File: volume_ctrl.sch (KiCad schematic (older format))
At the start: 40 parts, among them U1 TL072, U2 NE5532, U3 NE5532, U4 THAT2180

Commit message: Layout progress
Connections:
- net vca_in_R: now reaches R26.2, U4.1 (-)
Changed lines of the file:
@@
 EESchema Schematic File Version 4
+LIBS:AAMB-cache
 EELAYER 30 0
 EELAYER END
@@
 	1    0    0    -1
 $EndComp
+Text Label 6200 2425 0    50   ~ 0
+vca_in_R
 $EndSCHEMATC

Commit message: Lots of part changes to SMD devices. Adding MPN, MFG to all parts for BOM export.
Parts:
- C10, C9: MFG (none) -> Panasonic Electronic Components; MPN (none) -> EEV-FK1E102Q
- C11, C12: DigiKey (none) -> https://www.digikey.com/product-detail/en/w%C3%BCrth-elektr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; MFG (none) -> Würth Elektronik; MPN (none) -> 885012006053
- C13, C14, C7, C8: footprint Capacitor_THT:CP_Radial_D5.0mm_P2.00mm -> Capacitor_SMD:CP_Elec_5x3; DigiKey (none) -> https://www.digikey.com/product-detail/en/w%C3%BCrth-elektr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; MFG (none) -> Würth Elektronik; MPN (none) -> 865080642006
- C15, C16, C17, C18, C19, C20, C21, C22: MFG (none) -> KEMET; MPN (none) -> C0603C104Z3VACTU
- U4: MFG (none) -> Mill-Max Manufacturing Corp.; MPN (none) -> 214-99-316-01-670800
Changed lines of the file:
@@
 F 1 "THAT2180" H 6900 5100 50  0000 L CNN
 F 2 "Package_DIP:DIP-16_W7.62mm_SMDSocket_SmallPads" H 7100 4475 50  0001 C CNN
-F 3 "" H 7250 5275 50  0001 C CNN
+F 3 "https://www.mill-max.com/assets/pdfs/metric/108M.pdf" H 7250 5275 50  0001 C CNN
 F 4 "https://www.digikey.com/product-detail/en/mill-max-manufacturing-corp/214-99-316-01-670800/ED2130-ND/9895" H 6700 5225 50  0001 C CNN "DigiKey"
+F 5 "Mill-Max Manufacturing Corp." H 6700 5225 50  0001 C CNN "MFG"
+F 6 "214-99-316-01-670800" H 6700 5225 50  0001 C CNN "MPN"
 	2    6700 5225
 	1    0    0    -1
@@
 F 1 "THAT2180" H 6900 2300 50  0000 L CNN
 F 2 "Package_DIP:DIP-16_W7.62mm_SMDSocket_SmallPads" H 7100 1675 50  0001 C CNN
-F 3 "" H 7250 2475 50  0001 C CNN
+F 3 "https://www.mill-max.com/assets/pdfs/metric/108M.pdf" H 7250 2475 50  0001 C CNN
 F 4 "https://www.digikey.com/product-detail/en/mill-max-manufacturing-corp/214-99-316-01-670800/ED2130-ND/9895" H 6700 2425 50  0001 C CNN "DigiKey"
+F 5 "Mill-Max Manufacturing Corp." H 6700 2425 50  0001 C CNN "MFG"
+F 6 "214-99-316-01-670800" H 6700 2425 50  0001 C CNN "MPN"
 	1    6700 2425
 	1    0    0    -1
@@
 F 0 "C8" V 5370 5225 50  0000 C CNN
 F 1 "10u" V 5461 5225 50  0000 C CNN
-F 2 "Capacitor_THT:CP_Radial_D5.0mm_P2.00mm" H 5663 5075 50  0001 C CNN
-F 3 "~" H 5625 5225 50  0001 C CNN
+F 2 "Capacitor_SMD:CP_Elec_5x3" H 5663 5075 50  0001 C CNN
+F 3 "https://www.we-online.de/katalog/datasheet/865080642006.pdf" H 5625 5225 50  0001 C CNN
+F 4 "https://www.digikey.com/product-detail/en/w%C3%BCrth-elektronik/865080642006/732-8451-1-ND/5728408" H 5625 5225 50  0001 C CNN "DigiKey"
+F 5 "Würth Elektronik" H 5625 5225 50  0001 C CNN "MFG"
+F 6 "865080642006" H 5625 5225 50  0001 C CNN "MPN"
 	1    5625 5225
 	0    1    1    0
@@
 F 1 "22p" V 7500 5550 50  0000 C CNN
 F 2 "Capacitor_SMD:C_0603_1608Metric_Pad1.05x0.95mm_HandSolder" H 7763 5400 50  0001 C CNN
-F 3 "~" H 7725 5550 50  0001 C CNN
+F 3 "https://katalog.we-online.de/pbs/datasheet/885012006053.pdf" H 7725 5550 50  0001 C CNN
+F 4 "https://www.digikey.com/product-detail/en/w%C3%BCrth-elektronik/885012006053/732-7795-1-ND/5454422" H 7725 5550 50  0001 C CNN "DigiKey"
+F 5 "Würth Elektronik" H 7725 5550 50  0001 C CNN "MFG"
+F 6 "885012006053" H 7725 5550 50  0001 C CNN "MPN"
 	1    7725 5550
 	0    1    -1   0
@@
 F 0 "C14" V 9005 4850 50  0000 C CNN
 F 1 "10u" V 8914 4850 50  0000 C CNN
-F 2 "Capacitor_THT:CP_Radial_D5.0mm_P2.00mm" H 8788 4700 50  0001 C CNN
-F 3 "~" H 8750 4850 50  0001 C CNN
+F 2 "Capacitor_SMD:CP_Elec_5x3" H 8788 4700 50  0001 C CNN
+F 3 "https://www.we-online.de/katalog/datasheet/865080642006.pdf" H 8750 4850 50  0001 C CNN
+F 4 "https://www.digikey.com/product-detail/en/w%C3%BCrth-elektronik/865080642006/732-8451-1-ND/5728408" H 8750 4850 50  0001 C CNN "DigiKey"
+F 5 "Würth Elektronik" H 8750 4850 50  0001 C CNN "MFG"
+F 6 "865080642006" H 8750 4850 50  0001 C CNN "MPN"
 	1    8750 4850
 	0    -1   -1   0
@@
 F 3 "https://na.industrial.panasonic.com/file-download/3122" H 5850 3300 50  0001 C CNN
 F 4 "https://www.digikey.com/product-detail/en/panasonic-electronic-components/EEV-FK1E102Q/PCE3462TR-ND/396274" H 5850 3300 50  0001 C CNN "DigiKey"
+F 5 "Panasonic Electronic Components" H 5850 3300 50  0001 C CNN "MFG"
+F 6 "EEV-FK1E102Q" H 5850 3300 50  0001 C CNN "MPN"
 	1    5850 3300
 	1    0    0    -1
@@
 F 0 "C7" V 5370 2425 50  0000 C CNN
 F 1 "10u" V 5461 2425 50  0000 C CNN
-F 2 "Capacitor_THT:CP_Radial_D5.0mm_P2.00mm" H 5663 2275 50  0001 C CNN
-F 3 "~" H 5625 2425 50  0001 C CNN
+F 2 "Capacitor_SMD:CP_Elec_5x3" H 5663 2275 50  0001 C CNN
+F 3 "https://www.we-online.de/katalog/datasheet/865080642006.pdf" H 5625 2425 50  0001 C CNN
+F 4 "https://www.digikey.com/product-detail/en/w%C3%BCrth-elektronik/865080642006/732-8451-1-ND/5728408" H 5625 2425 50  0001 C CNN "DigiKey"
+F 5 "Würth Elektronik" H 5625 2425 50  0001 C CNN "MFG"
+F 6 "865080642006" H 5625 2425 50  0001 C CNN "MPN"
 	1    5625 2425
 	0    1    1    0
@@
 F 1 "22p" V 7500 2750 50  0000 C CNN
 F 2 "Capacitor_SMD:C_0603_1608Metric_Pad1.05x0.95mm_HandSolder" H 7763 2600 50  0001 C CNN
-F 3 "~" H 7725 2750 50  0001 C CNN
+F 3 "https://katalog.we-online.de/pbs/datasheet/885012006053.pdf" H 7725 2750 50  0001 C CNN
+F 4 "https://www.digikey.com/product-detail/en/w%C3%BCrth-elektronik/885012006053/732-7795-1-ND/5454422" H 7725 2750 50  0001 C CNN "DigiKey"
+F 5 "Würth Elektronik" H 7725 2750 50  0001 C CNN "MFG"
+F 6 "885012006053" H 7725 2750 50  0001 C CNN "MPN"
 	1    7725 2750
 	0    1    -1   0
@@
 F 3 "https://api.kemet.com/component-edge/download/datasheet/C0603C104Z3VACTU.pdf" H 900 950 50  0001 C CNN
 F 4 "https://www.digikey.com/product-detail/en/kemet/C0603C104Z3VACTU/399-1100-1-ND/411375" H 900 950 50  0001 C CNN "DigiKey"
+F 5 "KEMET" H 900 950 50  0001 C CNN "MFG"
+F 6 "C0603C104Z3VACTU" H 900 950 50  0001 C CNN "MPN"
 	1    900  950
 	1    0    0    -1
@@
 F 3 "https://api.kemet.com/component-edge/download/datasheet/C0603C104Z3VACTU.pdf" H 900 1300 50  0001 C CNN
 F 4 "https://www.digikey.com/product-detail/en/kemet/C0603C104Z3VACTU/399-1100-1-ND/411375" H 900 1300 50  0001 C CNN "DigiKey"
+F 5 "KEMET" H 900 1300 50  0001 C CNN "MFG"
+F 6 "C0603C104Z3VACTU" H 900 1300 50  0001 C CNN "MPN"
 	1    900  1300
 	1    0    0    -1
@@
 F 3 "https://api.kemet.com/component-edge/download/datasheet/C0603C104Z3VACTU.pdf" H 2275 950 50  0001 C CNN
 F 4 "https://www.digikey.com/product-detail/en/kemet/C0603C104Z3VACTU/399-1100-1-ND/411375" H 2275 950 50  0001 C CNN "DigiKey"
+F 5 "KEMET" H 2275 950 50  0001 C CNN "MFG"
+F 6 "C0603C104Z3VACTU" H 2275 950 50  0001 C CNN "MPN"
 	1    2275 950
 	-1   0    0    -1
@@
 F 3 "https://api.kemet.com/component-edge/download/datasheet/C0603C104Z3VACTU.pdf" H 2275 1300 50  0001 C CNN
 F 4 "https://www.digikey.com/product-detail/en/kemet/C0603C104Z3VACTU/399-1100-1-ND/411375" H 2275 1300 50  0001 C CNN "DigiKey"
+F 5 "KEMET" H 2275 1300 50  0001 C CNN "MFG"
+F 6 "C0603C104Z3VACTU" H 2275 1300 50  0001 C CNN "MPN"
 	1    2275 1300
 	-1   0    0    -1
@@
 F 3 "https://api.kemet.com/component-edge/download/datasheet/C0603C104Z3VACTU.pdf" H 2975 925 50  0001 C CNN
 F 4 "https://www.digikey.com/product-detail/en/kemet/C0603C104Z3VACTU/399-1100-1-ND/411375" H 2975 925 50  0001 C CNN "DigiKey"
+F 5 "KEMET" H 2975 925 50  0001 C CNN "MFG"
+F 6 "C0603C104Z3VACTU" H 2975 925 50  0001 C CNN "MPN"
 	1    2975 925
 	-1   0    0    -1
@@
 F 3 "https://api.kemet.com/component-edge/download/datasheet/C0603C104Z3VACTU.pdf" H 2975 1275 50  0001 C CNN
 F 4 "https://www.digikey.com/product-detail/en/kemet/C0603C104Z3VACTU/399-1100-1-ND/411375" H 2975 1275 50  0001 C CNN "DigiKey"
+F 5 "KEMET" H 2975 1275 50  0001 C CNN "MFG"
+F 6 "C0603C104Z3VACTU" H 2975 1275 50  0001 C CNN "MPN"
 	1    2975 1275
 	-1   0    0    -1
@@
 F 3 "https://api.kemet.com/component-edge/download/datasheet/C0603C104Z3VACTU.pdf" H 3475 925 50  0001 C CNN
 F 4 "https://www.digikey.com/product-detail/en/kemet/C0603C104Z3VACTU/399-1100-1-ND/411375" H 3475 925 50  0001 C CNN "DigiKey"
+F 5 "KEMET" H 3475 925 50  0001 C CNN "MFG"
+F 6 "C0603C104Z3VACTU" H 3475 925 50  0001 C CNN "MPN"
 	1    3475 925
 	1    0    0    -1
@@
 F 3 "https://api.kemet.com/component-edge/download/datasheet/C0603C104Z3VACTU.pdf" H 3475 1275 50  0001 C CNN
 F 4 "https://www.digikey.com/product-detail/en/kemet/C0603C104Z3VACTU/399-1100-1-ND/411375" H 3475 1275 50  0001 C CNN "DigiKey"
+F 5 "KEMET" H 3475 1275 50  0001 C CNN "MFG"
+F 6 "C0603C104Z3VACTU" H 3475 1275 50  0001 C CNN "MPN"
 	1    3475 1275
 	1    0    0    -1
@@
 F 0 "C13" V 9005 2050 50  0000 C CNN
 F 1 "10u" V 8914 2050 50  0000 C CNN
-F 2 "Capacitor_THT:CP_Radial_D5.0mm_P2.00mm" H 8788 1900 50  0001 C CNN
-F 3 "~" H 8750 2050 50  0001 C CNN
+F 2 "Capacitor_SMD:CP_Elec_5x3" H 8788 1900 50  0001 C CNN
+F 3 "https://www.we-online.de/katalog/datasheet/865080642006.pdf" H 8750 2050 50  0001 C CNN
+F 4 "https://www.digikey.com/product-detail/en/w%C3%BCrth-elektronik/865080642006/732-8451-1-ND/5728408" H 8750 2050 50  0001 C CNN "DigiKey"
+F 5 "Würth Elektronik" H 8750 2050 50  0001 C CNN "MFG"
+F 6 "865080642006" H 8750 2050 50  0001 C CNN "MPN"
 	1    8750 2050
 	0    -1   -1   0
@@
 F 3 "https://na.industrial.panasonic.com/file-download/3122" H 5850 6100 50  0001 C CNN
 F 4 "https://www.digikey.com/product-detail/en/panasonic-electronic-components/EEV-FK1E102Q/PCE3462TR-ND/396274" H 5850 6100 50  0001 C CNN "DigiKey"
+F 5 "Panasonic Electronic Components" H 5850 6100 50  0001 C CNN "MFG"
+F 6 "EEV-FK1E102Q" H 5850 6100 50  0001 C CNN "MPN"
 	1    5850 6100
 	1    0    0    -1

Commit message: Layout startover, sorting, some routing. Removed redundant fuses. BOM export.
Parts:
- C11, C12, C13, C14, C7, C8: MFG Würth Elektronik -> Wurth Elektronik
- R16, R17: DigiKey (none) -> https://www.digikey.com/product-detail/en/panasonic-electro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; MFG (none) -> Panasonic Electronic Components; MPN (none) -> ERJ-3EKF1501V
- R18, R25: DigiKey (none) -> https://www.digikey.com/product-detail/en/te-connectivity-p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; MFG (none) -> TE Connectivity Passive Product; MPN (none) -> CRGCQ0603F2K2
- R19: DigiKey (none) -> https://www.digikey.com/product-detail/en/panasonic-electro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; MFG (none) -> Panasonic Electronic Components; MPN (none) -> ERJ-3EKF1004V
- R20, R21, R28, R29, R34, R35: DigiKey (none) -> https://www.digikey.com/product-detail/en/vishay-dale/RCS06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; MFG (none) -> Vishay Dale; MPN (none) -> RCS0603100RFKEA
- R22, R23, R26, R27, R32, R33: DigiKey (none) -> https://www.digikey.com/product-detail/en/te-connectivity-p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; MFG (none) -> TE Connectivity Passive Product; MPN (none) -> CRGCQ0603F22K
- R30, R31: DigiKey (none) -> https://www.digikey.com/product-detail/en/panasonic-electro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; MFG (none) -> Panasonic Electronic Components; MPN (none) -> ERJ-PA3F5101V
- U1: DigiKey (none) -> https://www.digikey.com/product-detail/en/stmicroelectronic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; MFG (none) -> STMicroelectronics; MPN (none) -> TL072CDT
- U2, U3: DigiKey (none) -> https://www.digikey.com/product-detail/en/texas-instruments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; MFG (none) -> Texas Instruments; MPN (none) -> NE5532DR

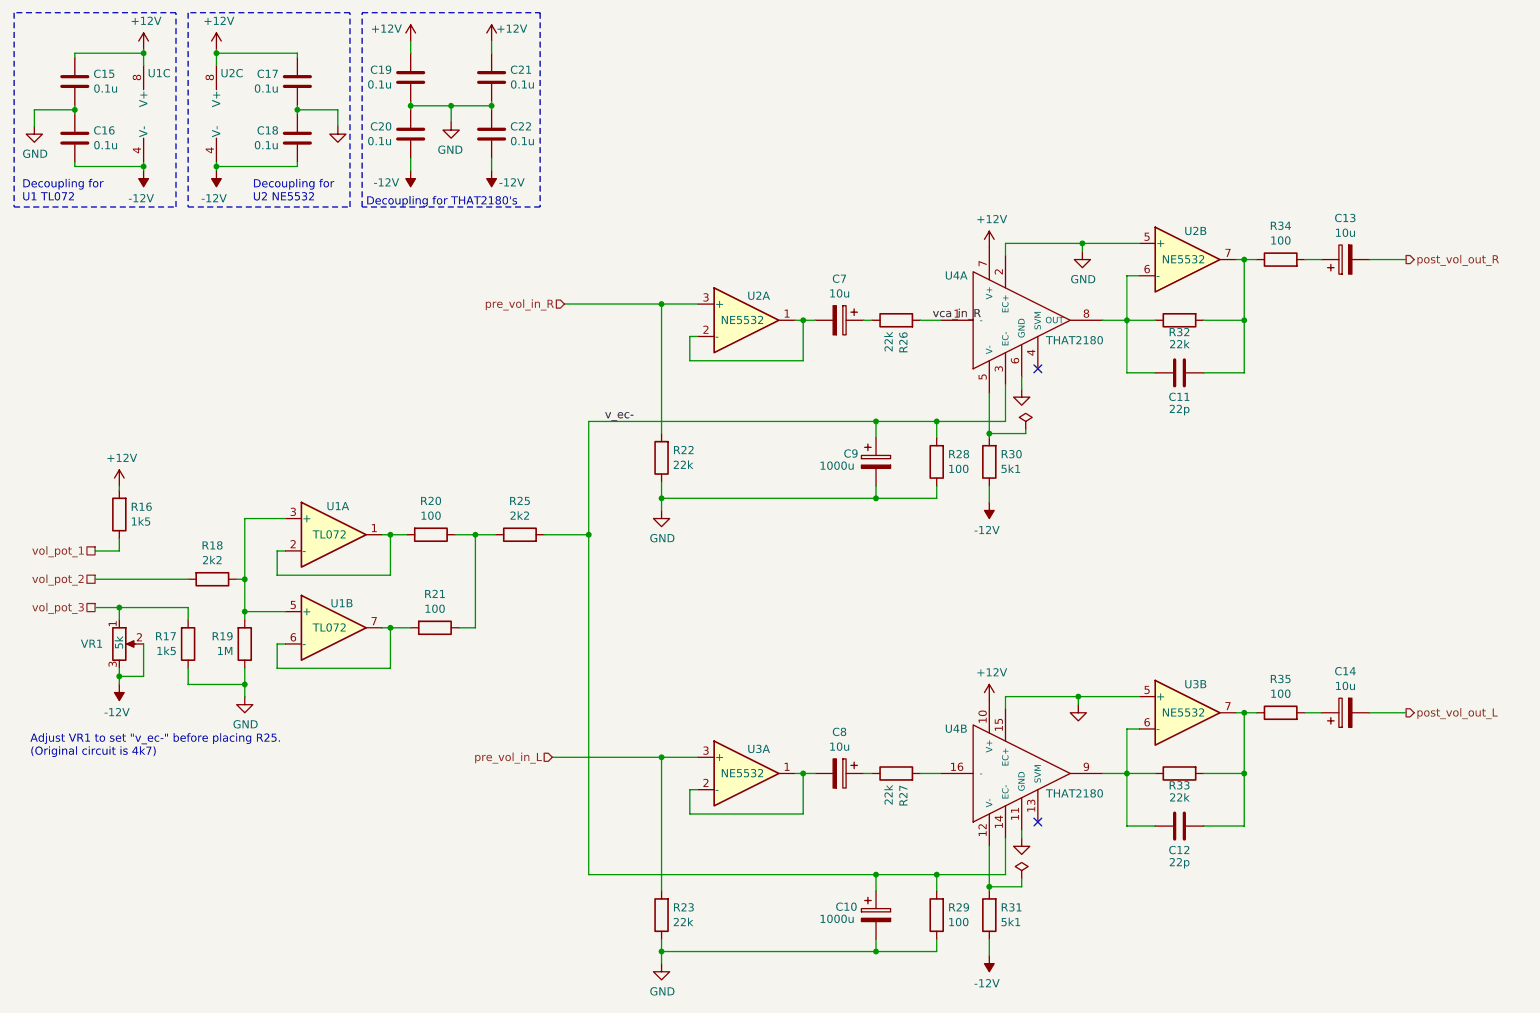
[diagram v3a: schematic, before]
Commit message: Layout progress. Added two missing decoupling caps.
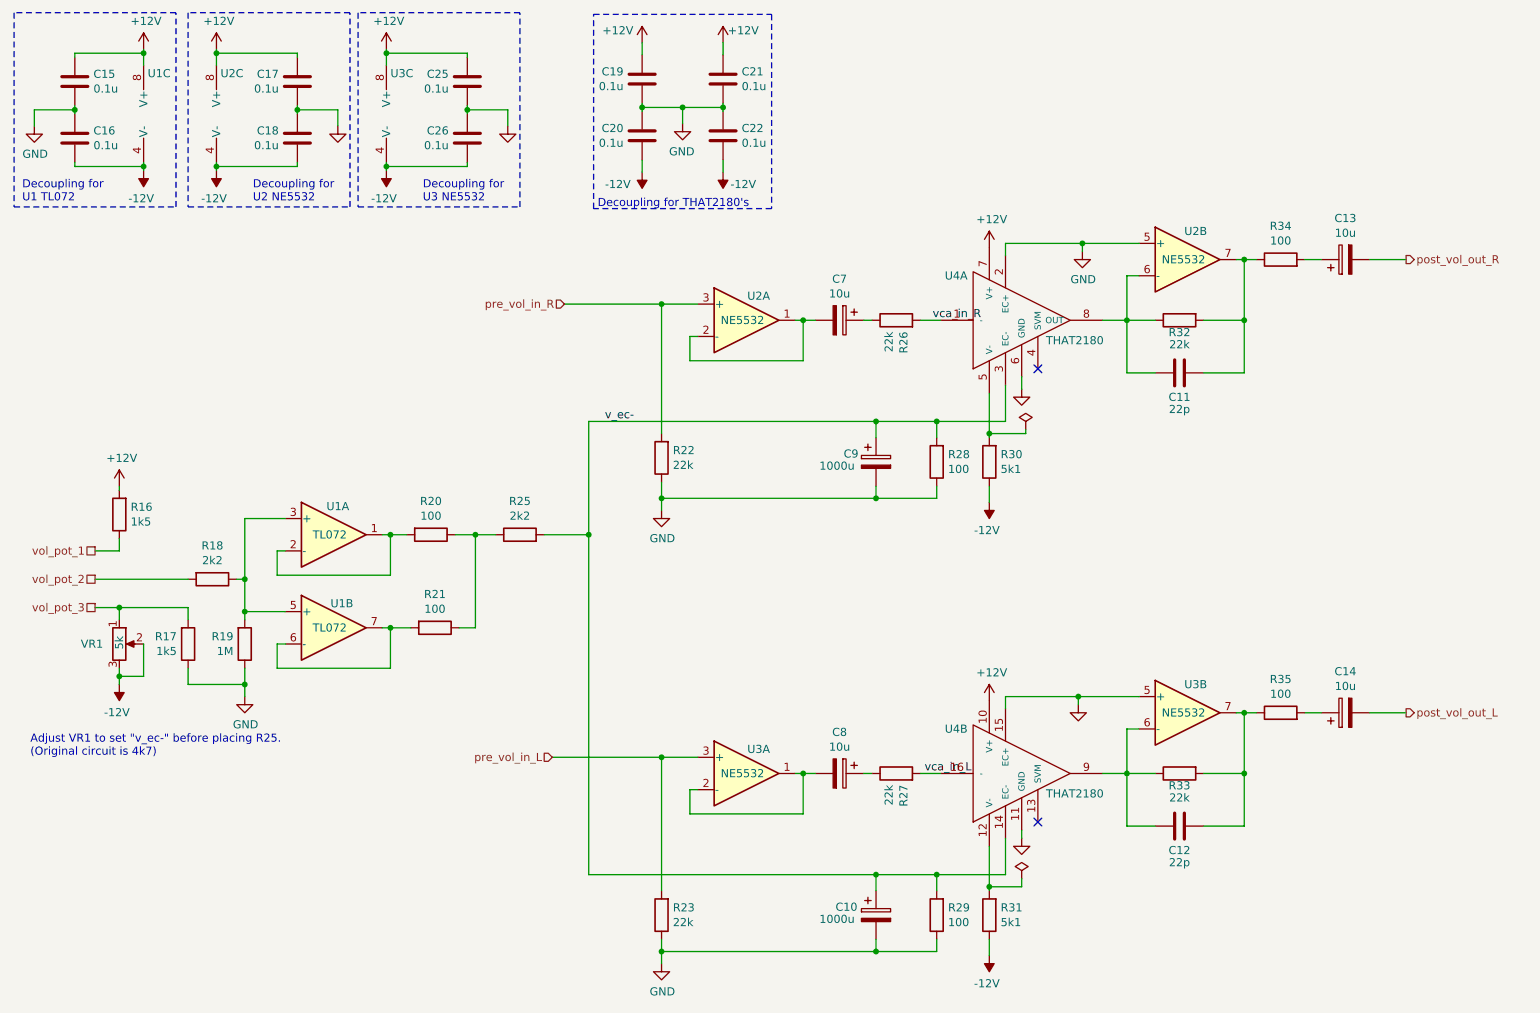
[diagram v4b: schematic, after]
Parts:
- added C25, C26: 0.1u, Capacitor_SMD:C_0603_1608Metric_Pad1.05x0.95mm_HandSolder, symbol Device:C
- added unit 3 of U3
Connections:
- net +12V: now also C25.1, U3.8 (V+)
- net -12V: now also C26.2, U3.4 (V-)
- net GND: now also C25.2, C26.1
- net vca_in_L: now reaches R27.2, U4.16 (-)
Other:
- note added: "Decoupling for \nU3 NE5532"
- moved on the sheet: C19, C20, C21, C22

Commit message: Place and route complete. Silkscreen cleanup needed.
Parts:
- VR1: footprint Murata-POT:PV36W202C01B00 -> Potentiometer_THT:Nidec_CT6EP202; DigiKey (none) -> https://www.digikey.com/products/en?keywords=CT6EP202; MFG (none) -> Nidec Copal Electronics; MPN (none) -> CT6EP202; Mouser https://www.mouser.com/ProductDetail/Bourns/PV36W502C01B00?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 -> (none)
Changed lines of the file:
@@
 F 0 "VR1" H 1075 4425 50  0000 R CNN
 F 1 "5k" V 1175 4475 50  0000 R CNN
-F 2 "Murata-POT:PV36W202C01B00" H 1175 4425 50  0001 C CNN
-F 3 "https://www.mouser.com/ProductDetail/Bourns/PV36W502C01B00?qs=BqPwLKJeIrffwfpi4cR%2Fyg%3D%3D&gclid=Cj0KCQiAvJXxBRCeARIsAMSkAprVNxrqciw2F2bbLEol0MFfB_kQMYkrvleaPlVNZV5jLL3ntUG4zu0aApSuEALw_wcB" H 1175 4425 50  0001 C CNN
-F 4 "https://www.mouser.com/ProductDetail/Bourns/PV36W502C01B00?qs=BqPwLKJeIrffwfpi4cR%2Fyg%3D%3D&gclid=Cj0KCQiAvJXxBRCeARIsAMSkAprVNxrqciw2F2bbLEol0MFfB_kQMYkrvleaPlVNZV5jLL3ntUG4zu0aApSuEALw_wcB" H 1175 4425 50  0001 C CNN "Mouser"
+F 2 "Potentiometer_THT:Nidec_CT6EP202" H 1175 4425 50  0001 C CNN
+F 3 "https://www.nidec-copal-electronics.com/e/catalog/trimmer/ct-6.pdf" H 1175 4425 50  0001 C CNN
+F 4 "https://www.digikey.com/products/en?keywords=CT6EP202" H 1175 4425 50  0001 C CNN "DigiKey"
+F 5 "Nidec Copal Electronics" H 1175 4425 50  0001 C CNN "MFG"
+F 6 "CT6EP202" H 1175 4425 50  0001 C CNN "MPN"
 	1    1175 4425
 	1    0    0    -1
